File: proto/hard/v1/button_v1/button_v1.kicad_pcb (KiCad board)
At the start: 2 copper layers, 108.9 x 76.9 mm, 149 parts, among them J1 Conn_01x06_Female, J10 Conn_01x05_Male, J14 K3-2235D, J2 Conn_01x06_Female, J3 Conn_01x06_Female, J4 Conn_01x06_Female, J5 USB_B_Micro, J6 Conn_01x08_Female, J7 Conn_01x04_Female, J8 AudioJack3, J9 Conn_01x06_Male, Q1 TP0610T, Q10 Q_NPN_BEC, Q11 Q_NPN_BEC, Q12 Q_NPN_BEC, Q13 Q_NPN_BEC, Q2 IRLML2060, Q3 TP0610T, Q4 IRLML2060, Q5 IRLML2060, Q6 UMG8N, Q7 UMG8N, Q8 IRLML2803, Q9 TP0610T, U1 LCD_2.8_SPI, U10 NL27WZ14, U11 TC305, U12 LCD_1_8_SPI, U13 74HC595, U2 STM32F103C8Tx, U3 RT8009-33, U4 RClamp0554S, U5 RT9293, U6 LM339, U7 AP1117-33, U8 485, U9 LM358, Y1 8MHz

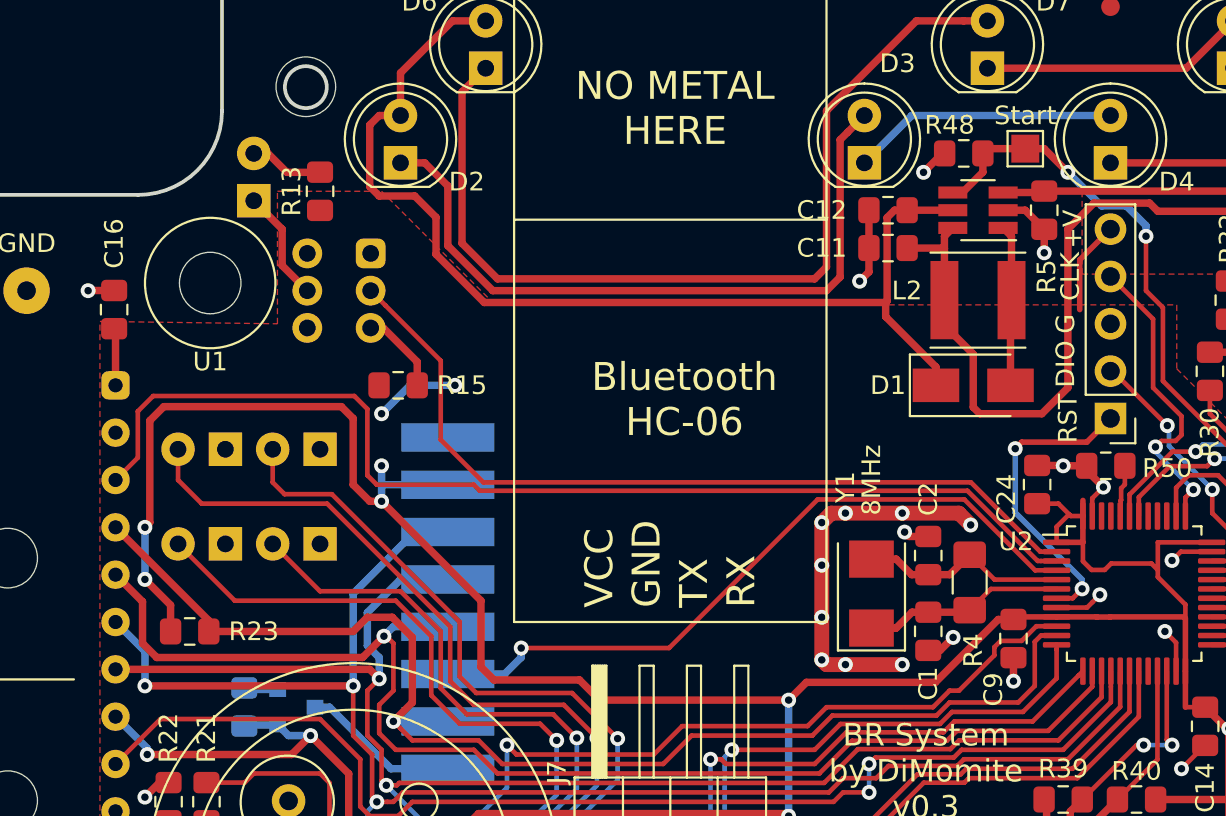
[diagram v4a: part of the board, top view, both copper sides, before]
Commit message: Added cap for back LCD. Modified traces to optimize power distribution.
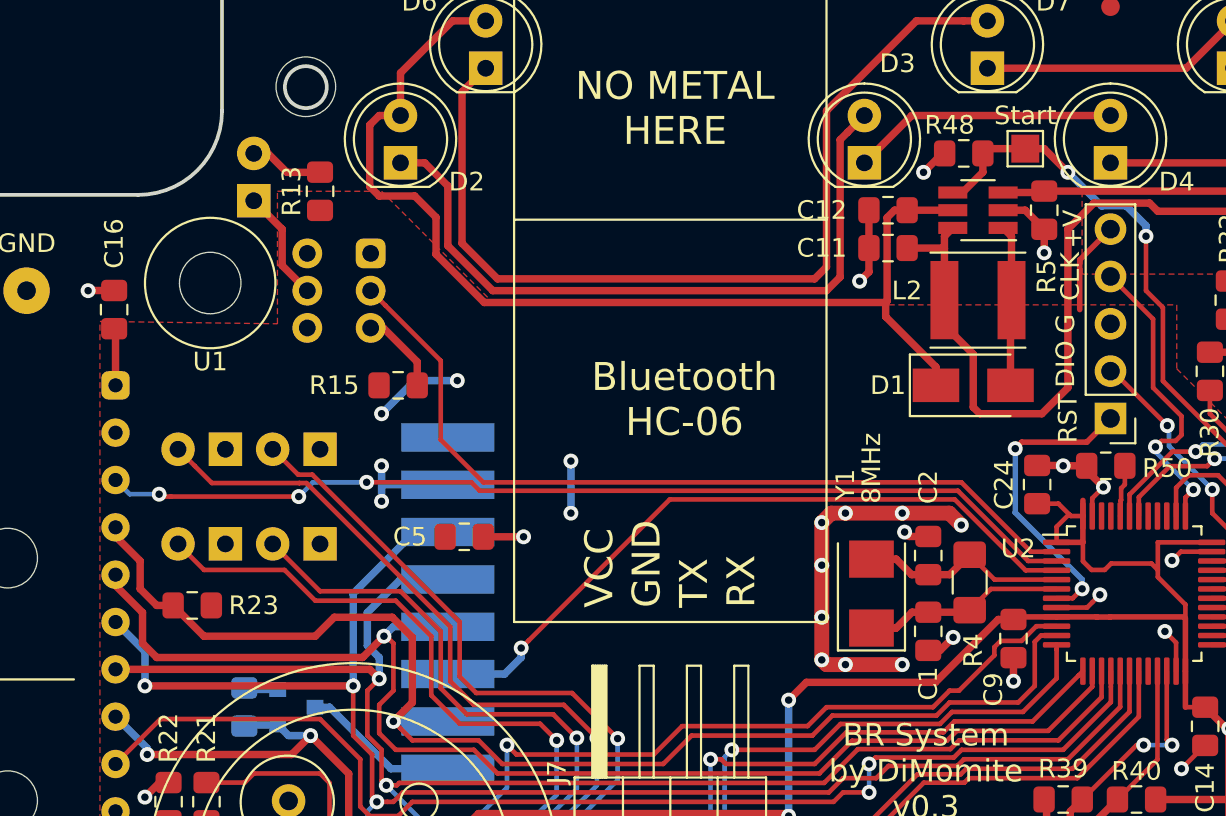
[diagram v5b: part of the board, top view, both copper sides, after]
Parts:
- added C5: 0.1uF, Capacitor_SMD:C_0805_2012Metric_Pad1.15x1.40mm_HandSolder, F.Cu at (96.4, 84.6)
- moved R23 1.40 mm to (81.8, 88.3), turned to 180 degrees
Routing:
- net +3V3: track 265.5 -> 211.2 mm
- net /LCD_CS: track 59.6 -> 52.9 mm, vias 0 -> 3
- net GND: track 142.7 -> 144.3 mm, vias 50 -> 51
- net Net-(D13-Pad2): track 43.3 -> 42.3 mm
- net /LCD_RESET: track 68.0 -> 69.0 mm
- net Net-(D11-Pad2): track 46.3 -> 45.3 mm
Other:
- board text added: "Touch enabled"

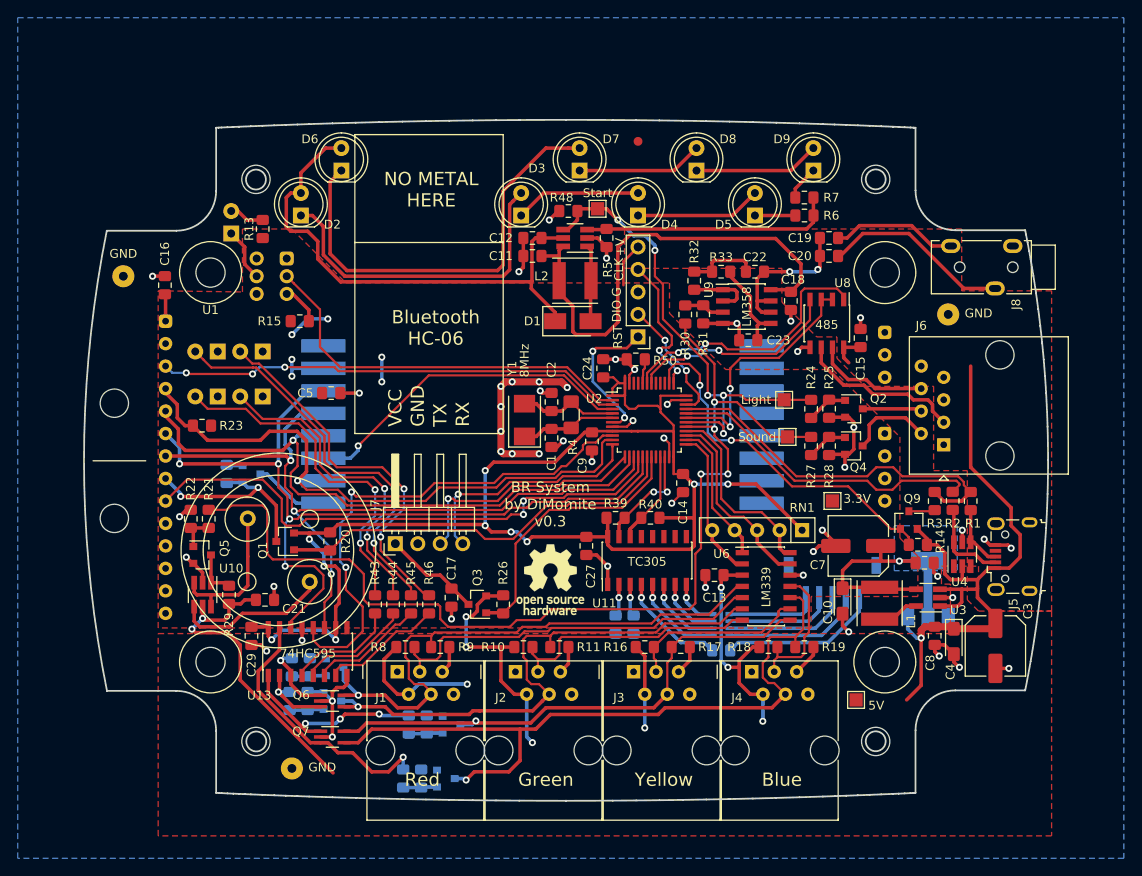
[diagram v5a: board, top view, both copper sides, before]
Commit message: Rework of main board prototype. Work not finished.
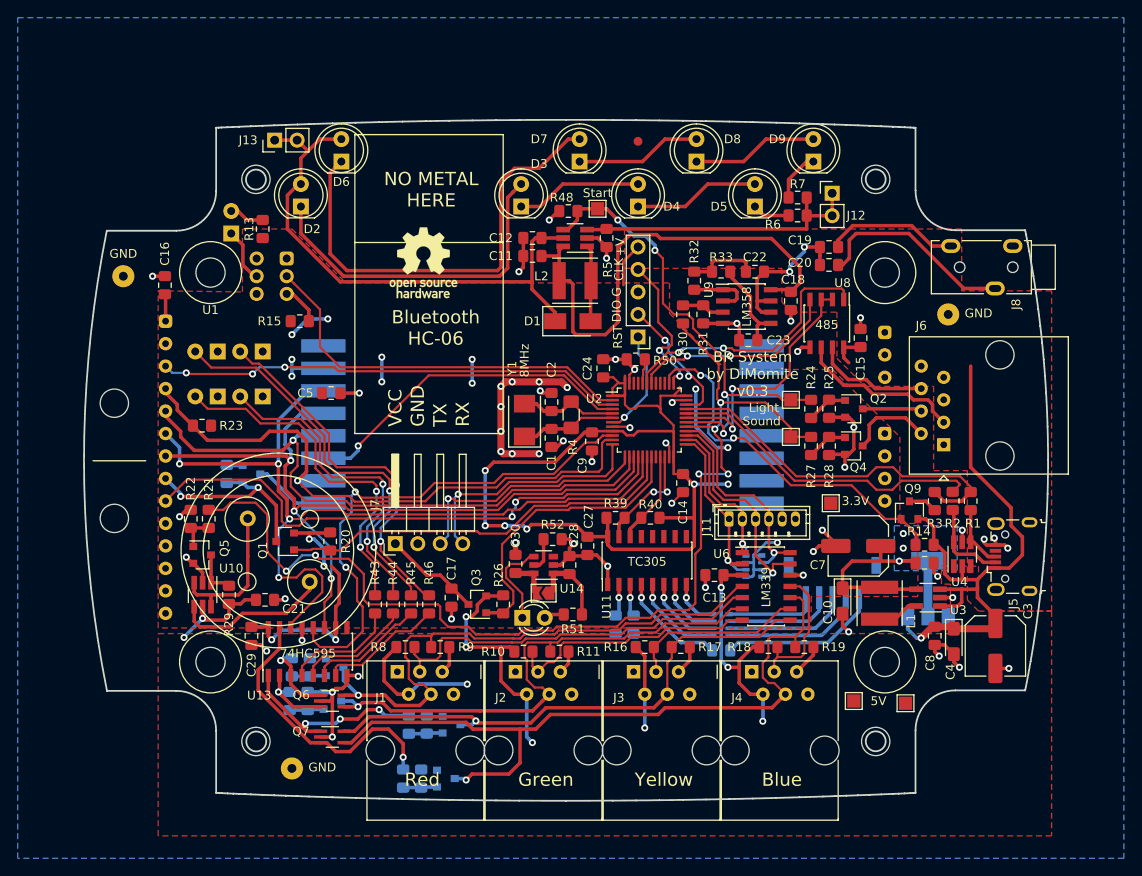
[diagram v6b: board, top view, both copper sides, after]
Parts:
- removed the REF** at (148.0, 89.5)
- removed the REF** at (155.7, 119.3)
- added C28: 0.1uF, Capacitor_SMD:C_0805_2012Metric_Pad1.15x1.40mm_HandSolder, F.Cu at (123.3, 104.0)
- added C30: 0.1uF, Capacitor_SMD:C_0805_2012Metric_Pad1.15x1.40mm_HandSolder, F.Cu at (117.2, 103.9)
- added D15: LED, LED_THT:LED_D3.0mm, F.Cu at (118.0, 110.0)
- added J11: Conn_01x06_Male, brbuttonsystem:JST_ZH_B6B-ZR_1x06_P1.50mm_Vertical, F.Cu at (141.4, 98.8)
- added J12: Conn_01x02_Female, Connector_PinHeader_2.54mm:PinHeader_1x02_P2.54mm_Vertical, F.Cu at (153.0, 62.0)
- added J13: Conn_01x02_Female, Connector_PinHeader_2.54mm:PinHeader_1x02_P2.54mm_Vertical, F.Cu at (90.0, 56.0)
- added JP1: SolderJumper_2_Open, Jumper:SolderJumper-2_P1.3mm_Open_TrianglePad1.0x1.5mm, F.Cu at (120.4, 107.2)
- added R51: 1k, Resistor_SMD:R_0805_2012Metric_Pad1.15x1.40mm_HandSolder, F.Cu at (123.7, 109.6)
- added R52: 130k 1%, Resistor_SMD:R_0805_2012Metric_Pad1.15x1.40mm_HandSolder, F.Cu at (121.4, 101.1)
- added REF**: 5V, TestPoint:TestPoint_Pad_1.5x1.5mm, F.Cu at (155.4, 119.4)
- added REF**: Sound, TestPoint:TestPoint_Pad_1.5x1.5mm, F.Cu at (148.3, 89.5)
- added REF**: 5V, TestPoint:TestPoint_Pad_1.5x1.5mm, F.Cu at (161.3, 119.6)
- added U14: TPS2553, Package_TO_SOT_SMD:SOT-23-6, F.Cu at (120.4, 104.0)
- RN1: value 4k7 -> 47k; footprint Resistor_THT:R_Array_SIP5 -> Resistor_SMD:R_Array_Convex_4x0603; moved to B.Cu
- U10: value NL27WZ14 -> SN74LVC2G04DBVR
- moved REF** 38.6 mm to (106.8, 69.8)
- moved RN1 6.80 mm to (144.2, 104.1), turned to 0 degrees
- moved Q9 1.13 mm to (161.7, 97.8)
- moved C19 1.02 mm to (152.6, 68.1)
- moved C20 1.02 mm to (152.6, 70.1)
- moved D2 1.02 mm to (93.0, 63.5)
- moved D3 1.02 mm to (117.9, 63.5)
- moved D4 1.02 mm to (131.1, 63.5)
- moved D5 1.02 mm to (144.3, 63.5)
- moved D6 1.02 mm to (97.5, 58.4)
- moved D7 1.02 mm to (124.5, 58.4)
- moved D8 1.02 mm to (137.7, 58.4)
- moved D9 1.02 mm to (150.9, 58.4)
- moved R6 0.77 mm to (149.1, 64.5)
- moved R14 0.76 mm to (163.4, 101.7)
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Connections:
- RN1 pad 2: /But3 -> /But0
- RN1 pad 3: /But2 -> +3V3
- RN1 pad 5: /But0 -> +3V3
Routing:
- net +5V: track 250.5 -> 229.5 mm
- net /Buttons/BUT_POWER_FAULT: track 0.00 -> 10.0 mm
- net GND: track 144.3 -> 153.2 mm, vias 51 -> 55
- net +3V3: track 211.2 -> 204.6 mm, vias 17 -> 24
- net Net-(J12-Pad1): track 28.7 -> 33.8 mm
- net +5VP: track 0.00 -> 4.46 mm
- net /NRST: track 16.4 -> 12.1 mm, vias 2 -> 1
- net /But2: track 22.0 -> 26.2 mm, vias 0 -> 1
- net /Entertainment/StartLedOut: track 58.4 -> 62.4 mm
- net Net-(R52-Pad1): track 0.00 -> 3.74 mm
- net /Sound_PWM: track 120.2 -> 123.3 mm, vias 4 -> 6
- net /LCD_MOSI: track 95.1 -> 98.0 mm
- net /But0: track 17.2 -> 20.0 mm, vias 0 -> 1
- net /But3: track 21.9 -> 24.5 mm, vias 0 -> 1
- net Net-(D15-Pad2): track 0.00 -> 2.31 mm
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
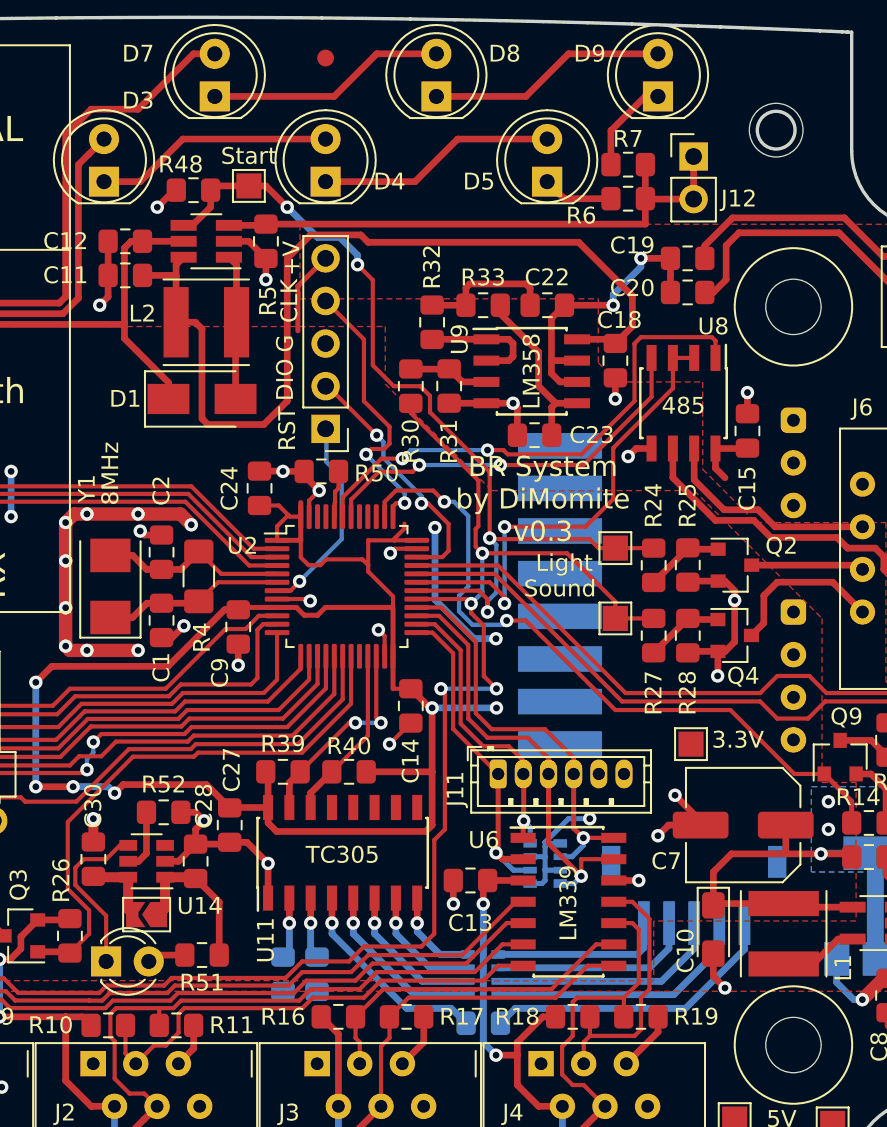
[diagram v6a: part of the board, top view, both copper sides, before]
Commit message: Main PCB changes: - replaced flashing connected with 6-pin version. One of which should be removed. This is done to make flashing by not skilled pesons safer. Corresponding connector on programmer will have jammed hole. - moved connected for touch buttons lower. This should give more free space for wireless module connector.
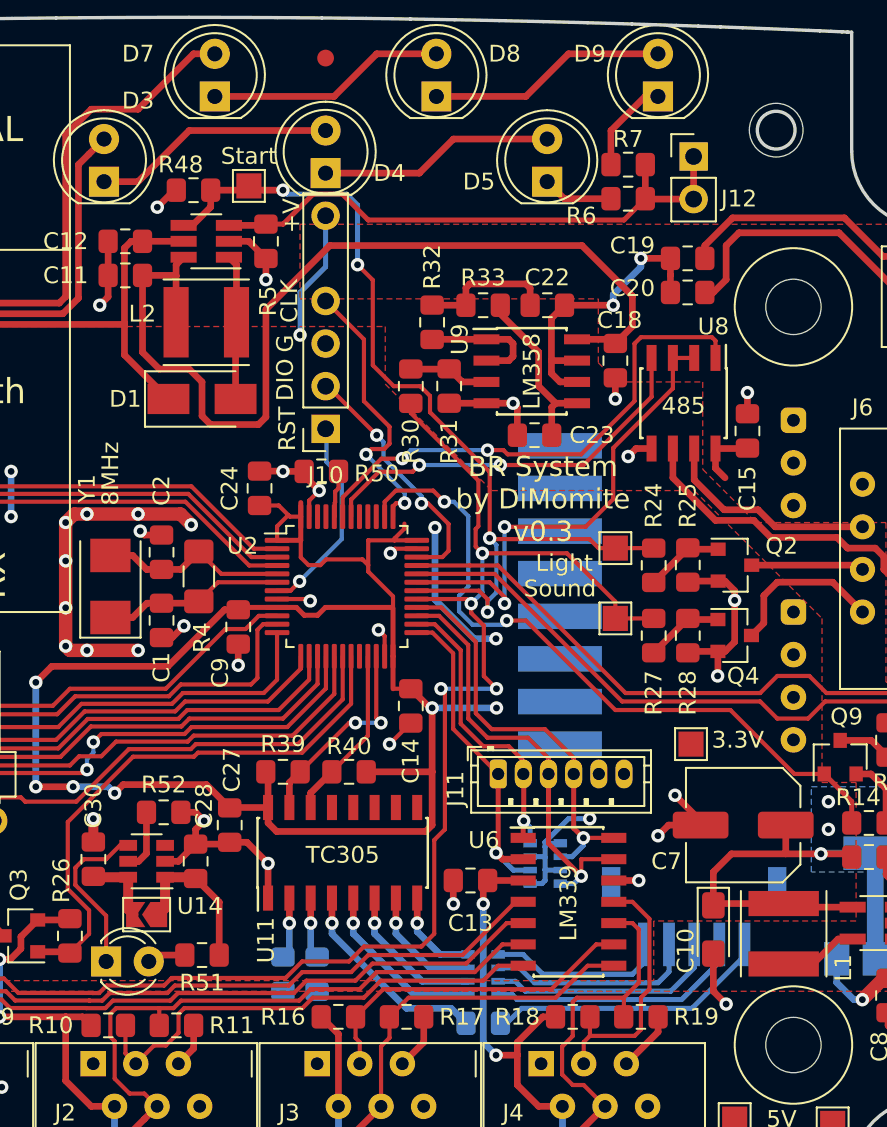
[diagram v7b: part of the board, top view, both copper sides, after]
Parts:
- J10: value Conn_01x05_Male -> Conn_01x06_Male; footprint Connector_PinHeader_2.54mm:PinHeader_1x05_P2.54mm_Vertical -> Connector_PinSocket_2.54mm:PinSocket_1x06_P2.54mm_Vertical
- moved J9 1.27 mm to (153.0, 109.0)
- moved D4 0.51 mm to (131.1, 63.0)
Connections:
- J10 pad 5: +3V3 -> Net-(J10-Pad5)
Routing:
- net +3V3: track 204.6 -> 207.3 mm, vias 24 -> 25
- net +5V: track 229.5 -> 231.7 mm
- net /StartLed: track 54.9 -> 56.7 mm
- net /CX0: track 17.9 -> 16.9 mm
- net GND: track 153.2 -> 154.2 mm
- net /CX1: track 15.9 -> 15.3 mm
